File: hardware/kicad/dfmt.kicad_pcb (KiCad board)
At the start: 2 copper layers, 50 x 50 mm, 38 parts, among them IC1 SI4735-D60, IC2 SI4735-D60, IC3 LE33-SMT, P1 FM ANT, P2 AM ANT, P3 PROG, P4 USB_B, SW1 UP, SW2 DOWN, Y1 8MHz

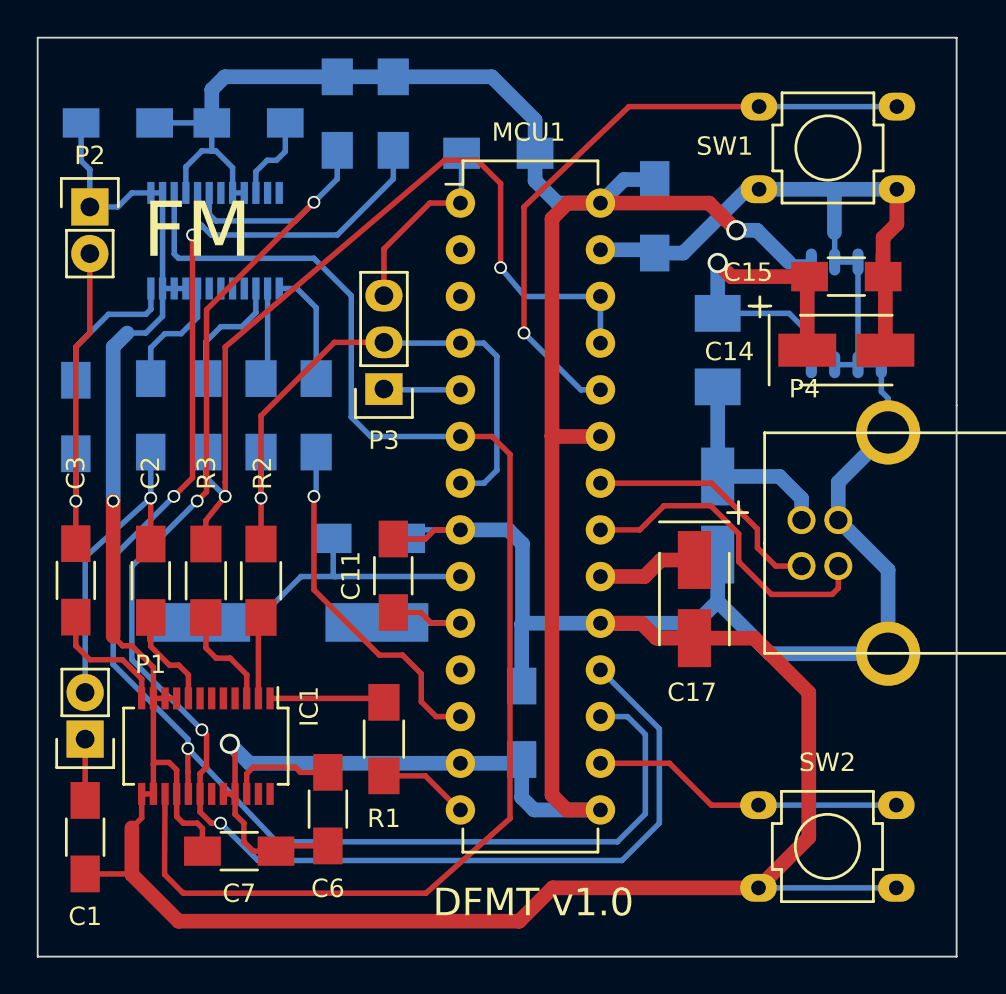
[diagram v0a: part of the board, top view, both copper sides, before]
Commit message: Added two holes.
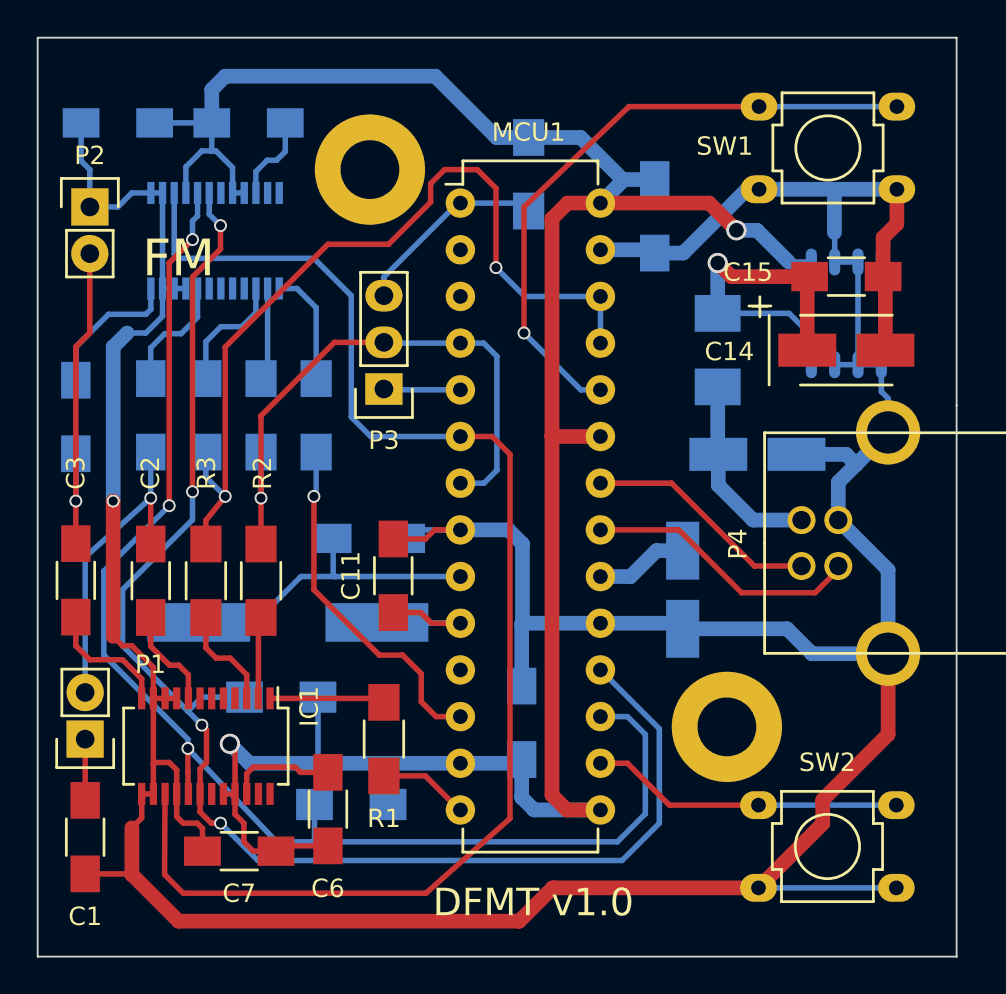
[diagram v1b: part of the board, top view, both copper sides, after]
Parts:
- added ?: SolderWirePad_single_2-5mmDrill, dfmt:MountHole_3.2mm, F.Cu at (262.6, 57.7)
- added ?: SolderWirePad_single_2-5mmDrill, dfmt:MountHole_3.2mm, F.Cu at (243.1, 27.2)
- C17: moved to B.Cu
- moved R9 37.7 mm to (242.1, 61.7), turned to 180 degrees
- moved R8 31.9 mm to (238.3, 55.9), turned to 180 degrees
- moved C13 3.97 mm to (264.2, 42.7), turned to 0 degrees
- moved R7 2.01 mm to (251.7, 27.4), turned to 270 degrees
- moved C17 0.81 mm to (260.1, 50.0)
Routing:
- net /SCLK: track 84.8 -> 73.6 mm
- net GND: track 233.1 -> 223.3 mm
- net /SDA: track 86.5 -> 78.2 mm
- net VDD: track 130.2 -> 135.1 mm
- net Net-(MCU1-Pad21): track 17.7 -> 15.1 mm
- net Net-(MCU1-Pad22): track 13.4 -> 12.8 mm
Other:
- rule pad_to_mask_clearance: 0 -> 0.15
- board text added: "SW-LW"
- board text removed: "AM"

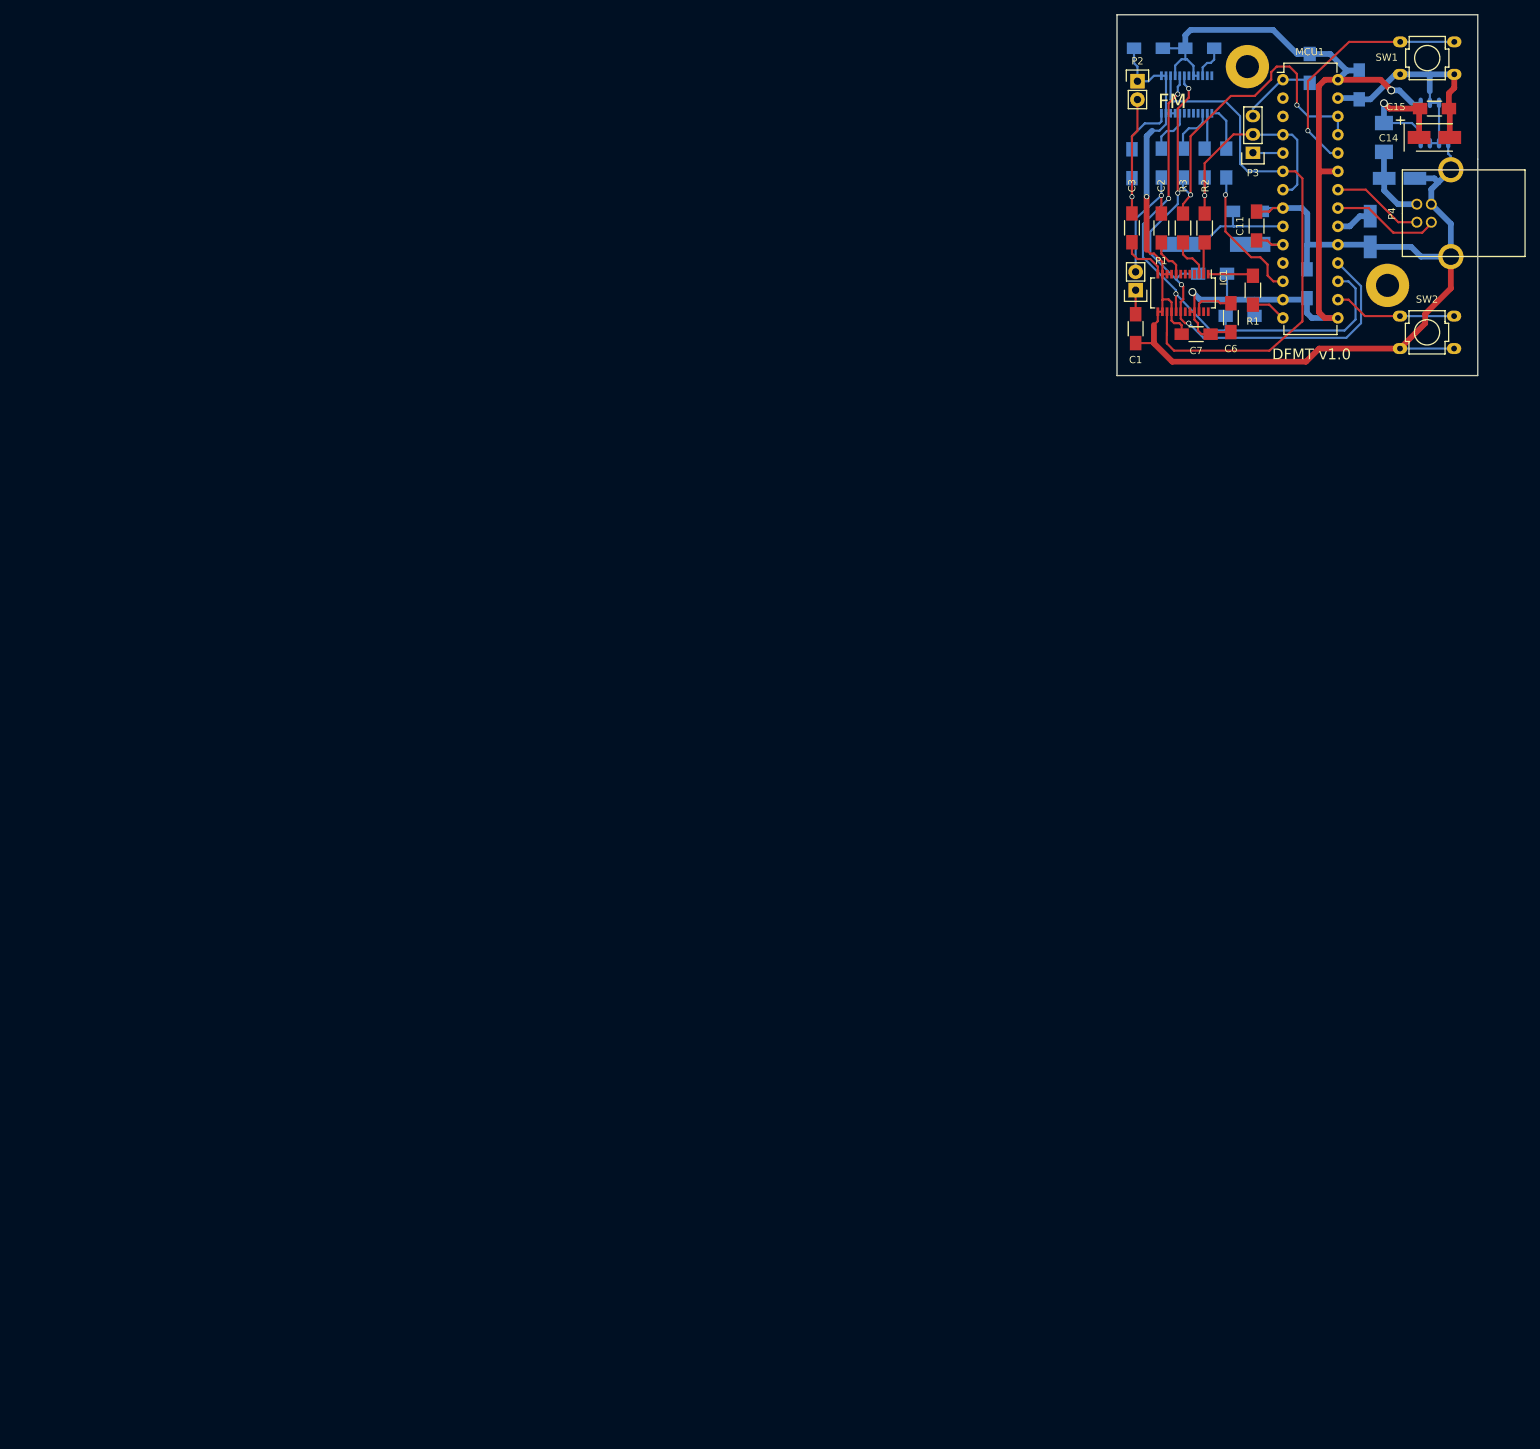
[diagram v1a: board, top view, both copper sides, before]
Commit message: HW v1.0 sent to fab. USB connector was modified to not go outside of PCB. Actual pictures was made. Updated schematic pdf wit new USB con. Added gerber and excelon files.
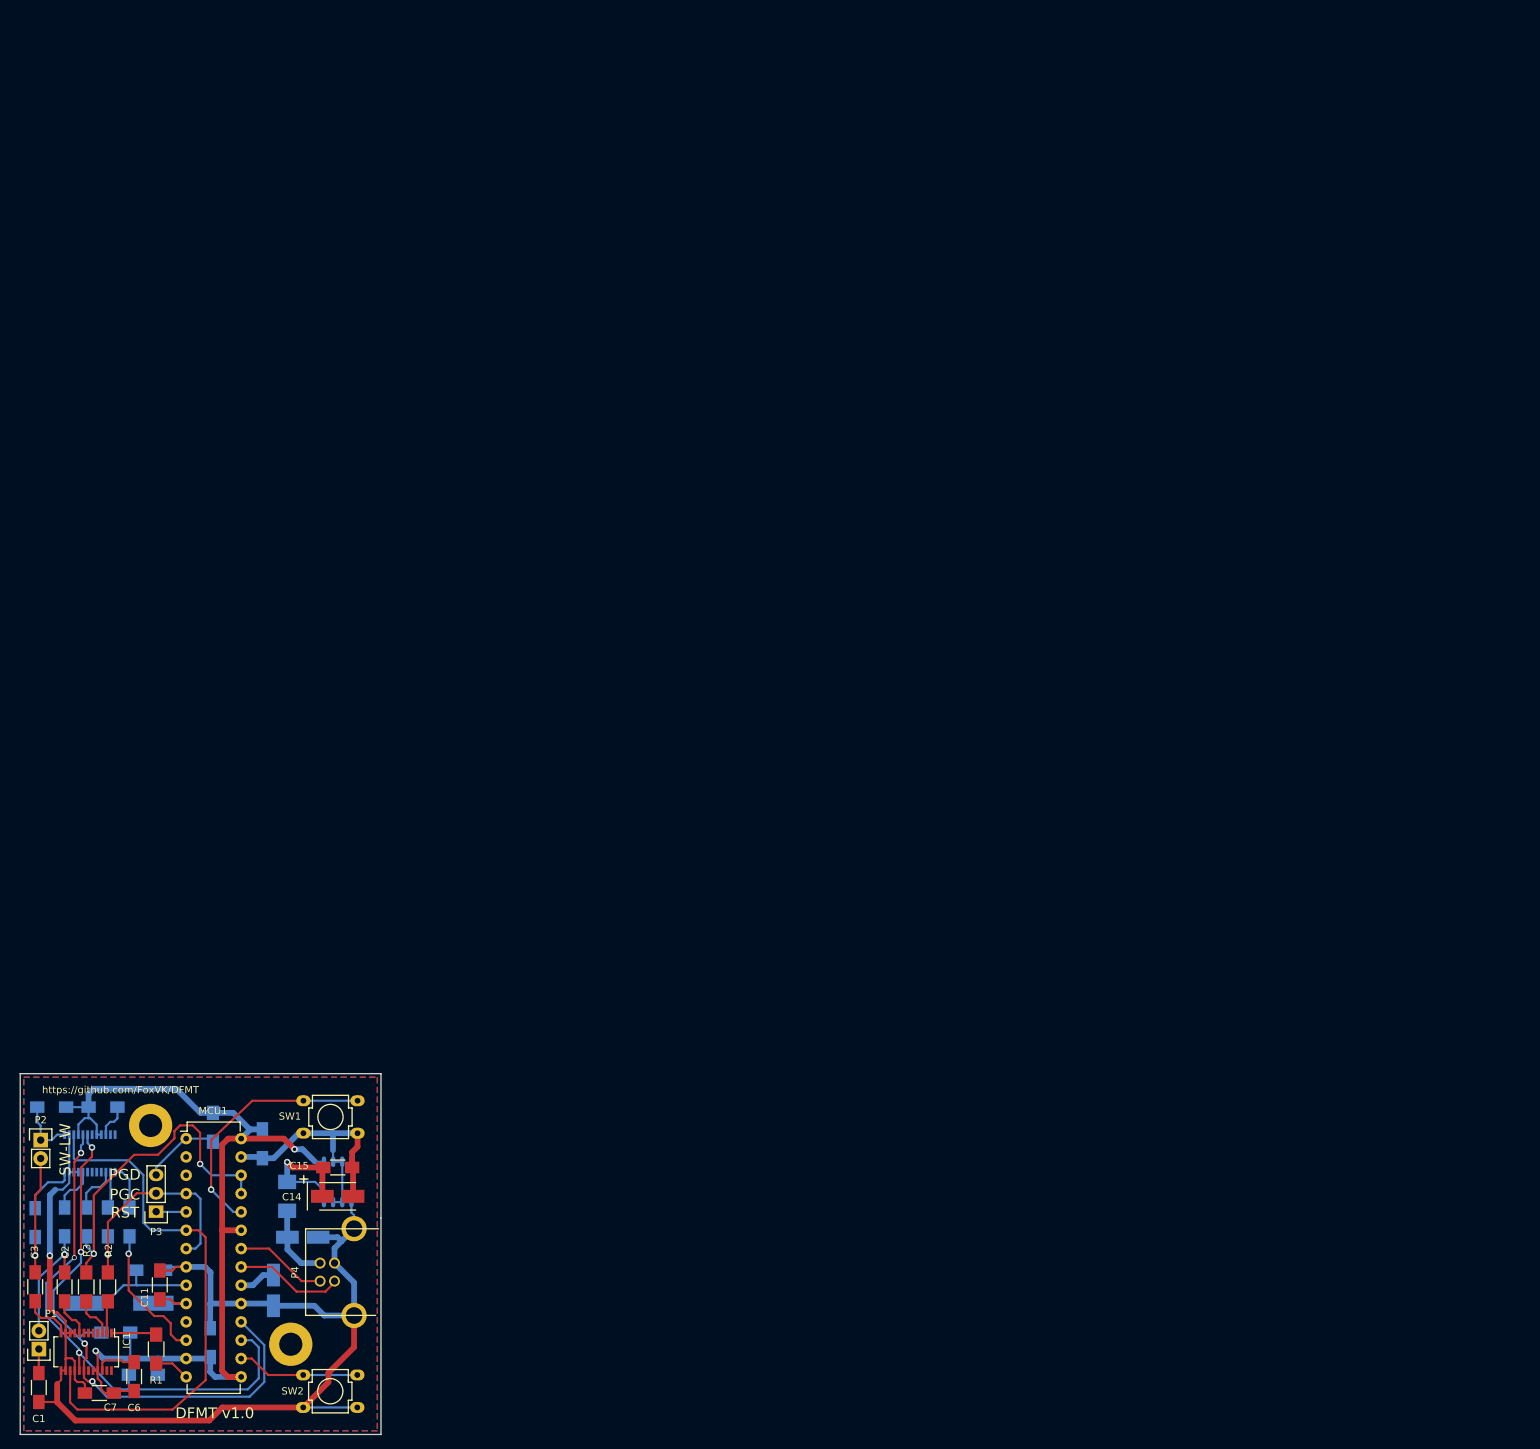
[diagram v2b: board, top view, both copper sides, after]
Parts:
- ? (x2): value SolderWirePad_single_2-5mmDrill -> (none)
- P4: footprint dfmt:USB20_B_F_molex_tht_kink -> dfmt:USB20_B_F_molex_tht_kink_cuted
- moved ? 211.3 mm to (110.6, 204.4)
- moved ? 211.3 mm to (91.1, 173.9)
- moved C1 211.3 mm to (75.6, 210.2)
- moved C10 211.3 mm to (91.1, 194.0)
- moved C11 211.3 mm to (92.3, 196.0)
- moved C12 211.3 mm to (99.3, 204.0)
- moved C13 211.3 mm to (112.2, 189.4)
- moved C14 211.3 mm to (117.0, 183.8)
- moved C15 211.3 mm to (117.0, 179.8)
- moved C16 211.3 mm to (106.6, 176.5)
- moved C17 211.3 mm to (108.1, 196.8)
- moved C2 211.3 mm to (79.2, 196.3)
- moved C3 211.3 mm to (75.1, 196.3)
- moved C4 211.3 mm to (79.2, 187.3)
- moved C5 211.3 mm to (75.1, 187.4)
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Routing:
- added copper zone on B.Cu, net GND
- added copper zone on F.Cu, net GND
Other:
- net class Default: via_dia 0.7 -> 0.9
- net class Power: via_dia 1 -> 1.2
- board text added: "PGC"
- board text added: "PGD"
- board text added: "RST"
- board text added: "https://github.com/FoxVK/DFMT"
